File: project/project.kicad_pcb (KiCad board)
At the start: 2 copper layers, 313 parts, among them J101 XT-IN, J102 IN, J103 5V, J104 OUT, J1501 RJ45_LED_Shielded_x2, J201 RJ45_LED_Shielded_x2, J2801 RJ45_LED_Shielded_x2, Q1001 AO3400A, Q101 HYG210P06LQ1D, Q1101 AO3400A, Q1201 AO3400A, Q1301 AO3400A, Q1401 AO3400A, Q1601 AO3400A, Q1701 AO3400A, Q1801 AO3400A, Q1901 AO3400A, Q2001 AO3400A, Q2101 AO3400A, Q2201 AO3400A, Q2301 AO3400A, Q2401 AO3400A, Q2501 AO3400A, Q2601 AO3400A, Q2701 AO3400A, Q2901 AO3400A, Q3001 AO3400A, Q301 AO3400A, Q3101 AO3400A, Q3201 AO3400A, Q3301 AO3400A, Q3401 AO3400A, Q3501 AO3400A, Q3601 AO3400A, Q3701 AO3400A, Q3801 AO3400A, Q3901 AO3400A, Q4001 AO3400A, Q401 AO3400A, Q501 AO3400A, Q601 AO3400A, Q701 AO3400A, Q801 AO3400A, Q901 AO3400A, U101 XL4001, U1501 PCA9685PW, U201 PCA9685PW, U2801 PCA9685PW

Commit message: 2ch grouping layout
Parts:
- moved J102 171.4 mm to (428.0, -91.9)
- moved J104 101.9 mm to (270.0, -119.9)
- moved R2804 50.2 mm to (466.9, -39.8)
- moved R2805 41.8 mm to (466.9, -37.8)
- moved R2803 32.5 mm to (479.4, -43.2), turned to 180 degrees
- moved R2802 30.6 mm to (479.4, -41.3), turned to 180 degrees
- moved C2801 11.5 mm to (479.4, -47.1)
- moved R2801 11.4 mm to (479.4, -45.1), turned to 180 degrees
- moved U2801 5.51 mm to (473.0, -42.0)
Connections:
- R1502 pad 2: /_double_port_pwr2/LED12 -> /_double_port_pwr2/LED21
- R1503 pad 2: /_double_port_pwr2/LED11 -> /_double_port_pwr2/LED22
- R1504 pad 2: /_double_port_pwr2/LED22 -> /_double_port_pwr2/LED11
- R1505 pad 2: /_double_port_pwr2/LED21 -> /_double_port_pwr2/LED12
- R202 pad 2: /_double_port_pwr1/LED12 -> /_double_port_pwr1/LED21
- R203 pad 2: /_double_port_pwr1/LED11 -> /_double_port_pwr1/LED22
- R204 pad 2: /_double_port_pwr1/LED22 -> /_double_port_pwr1/LED11
- R205 pad 2: /_double_port_pwr1/LED21 -> /_double_port_pwr1/LED12
- R2802 pad 2: /_double_port_pwr3/LED12 -> /_double_port_pwr3/LED21
- R2803 pad 2: /_double_port_pwr3/LED11 -> /_double_port_pwr3/LED22
- R2804 pad 2: /_double_port_pwr3/LED22 -> /_double_port_pwr3/LED11
- R2805 pad 2: /_double_port_pwr3/LED21 -> /_double_port_pwr3/LED12
- U1501 pad 10: /_double_port_pwr2/_single_channel_pwr_18/IN -> /_double_port_pwr2/_single_channel_pwr_23/IN
- U1501 pad 11: /_double_port_pwr2/_single_channel_pwr_22/IN -> /_double_port_pwr2/_single_channel_pwr_19/IN
- U1501 pad 15: /_double_port_pwr2/_single_channel_pwr_19/IN -> /_double_port_pwr2/_single_channel_pwr_22/IN
- U1501 pad 16: /_double_port_pwr2/_single_channel_pwr_23/IN -> /_double_port_pwr2/_single_channel_pwr_18/IN
- U1501 pad 17: /_double_port_pwr2/_single_channel_pwr_24/IN -> /_double_port_pwr2/_single_channel_pwr_21/IN
- U1501 pad 18: /_double_port_pwr2/_single_channel_pwr_14/IN -> /_double_port_pwr2/_single_channel_pwr_20/IN
- U1501 pad 19: /_double_port_pwr2/_single_channel_pwr_13/IN -> /_double_port_pwr2/_single_channel_pwr_17/IN
- U1501 pad 20: /_double_port_pwr2/_single_channel_pwr_15/IN -> /_double_port_pwr2/_single_channel_pwr_16/IN
- U1501 pad 6: /_double_port_pwr2/_single_channel_pwr_16/IN -> /_double_port_pwr2/_single_channel_pwr_15/IN
- U1501 pad 7: /_double_port_pwr2/_single_channel_pwr_17/IN -> /_double_port_pwr2/_single_channel_pwr_13/IN
- U1501 pad 8: /_double_port_pwr2/_single_channel_pwr_20/IN -> /_double_port_pwr2/_single_channel_pwr_14/IN
- U1501 pad 9: /_double_port_pwr2/_single_channel_pwr_21/IN -> /_double_port_pwr2/_single_channel_pwr_24/IN
- U201 pad 10: /_double_port_pwr1/_single_channel_pwr_18/IN -> /_double_port_pwr1/_single_channel_pwr_23/IN
- U201 pad 11: /_double_port_pwr1/_single_channel_pwr_22/IN -> /_double_port_pwr1/_single_channel_pwr_19/IN
- U201 pad 15: /_double_port_pwr1/_single_channel_pwr_19/IN -> /_double_port_pwr1/_single_channel_pwr_22/IN
- U201 pad 16: /_double_port_pwr1/_single_channel_pwr_23/IN -> /_double_port_pwr1/_single_channel_pwr_18/IN
- U201 pad 17: /_double_port_pwr1/_single_channel_pwr_24/IN -> /_double_port_pwr1/_single_channel_pwr_21/IN
- U201 pad 18: /_double_port_pwr1/_single_channel_pwr_14/IN -> /_double_port_pwr1/_single_channel_pwr_20/IN
- U201 pad 19: /_double_port_pwr1/_single_channel_pwr_13/IN -> /_double_port_pwr1/_single_channel_pwr_17/IN
- U201 pad 20: /_double_port_pwr1/_single_channel_pwr_15/IN -> /_double_port_pwr1/_single_channel_pwr_16/IN
- U201 pad 6: /_double_port_pwr1/_single_channel_pwr_16/IN -> /_double_port_pwr1/_single_channel_pwr_15/IN
- U201 pad 7: /_double_port_pwr1/_single_channel_pwr_17/IN -> /_double_port_pwr1/_single_channel_pwr_13/IN
- U201 pad 8: /_double_port_pwr1/_single_channel_pwr_20/IN -> /_double_port_pwr1/_single_channel_pwr_14/IN
- U201 pad 9: /_double_port_pwr1/_single_channel_pwr_21/IN -> /_double_port_pwr1/_single_channel_pwr_24/IN
- U2801 pad 10: /_double_port_pwr3/_single_channel_pwr_18/IN -> /_double_port_pwr3/_single_channel_pwr_23/IN
- U2801 pad 11: /_double_port_pwr3/_single_channel_pwr_22/IN -> /_double_port_pwr3/_single_channel_pwr_19/IN
- U2801 pad 15: /_double_port_pwr3/_single_channel_pwr_19/IN -> /_double_port_pwr3/_single_channel_pwr_22/IN
- U2801 pad 16: /_double_port_pwr3/_single_channel_pwr_23/IN -> /_double_port_pwr3/_single_channel_pwr_18/IN
- U2801 pad 17: /_double_port_pwr3/_single_channel_pwr_24/IN -> /_double_port_pwr3/_single_channel_pwr_21/IN
- U2801 pad 18: /_double_port_pwr3/_single_channel_pwr_14/IN -> /_double_port_pwr3/_single_channel_pwr_20/IN
- U2801 pad 19: /_double_port_pwr3/_single_channel_pwr_13/IN -> /_double_port_pwr3/_single_channel_pwr_17/IN
- U2801 pad 20: /_double_port_pwr3/_single_channel_pwr_15/IN -> /_double_port_pwr3/_single_channel_pwr_16/IN
- U2801 pad 6: /_double_port_pwr3/_single_channel_pwr_16/IN -> /_double_port_pwr3/_single_channel_pwr_15/IN
- U2801 pad 7: /_double_port_pwr3/_single_channel_pwr_17/IN -> /_double_port_pwr3/_single_channel_pwr_13/IN
- U2801 pad 8: /_double_port_pwr3/_single_channel_pwr_20/IN -> /_double_port_pwr3/_single_channel_pwr_14/IN
- U2801 pad 9: /_double_port_pwr3/_single_channel_pwr_21/IN -> /_double_port_pwr3/_single_channel_pwr_24/IN
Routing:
- net Net-(J2801-Pad12): track 0.00 -> 44.3 mm, vias 0 -> 1
- net Net-(J2801-Pad10): track 0.00 -> 41.2 mm, vias 0 -> 1
- net Net-(J2801-Pad22): track 0.00 -> 38.9 mm, vias 0 -> 1
- net Net-(J2801-Pad24): track 0.00 -> 38.2 mm, vias 0 -> 1
- net /_double_port_pwr3/_single_channel_pwr_16/IN: track 0.00 -> 32.2 mm
- net /_double_port_pwr3/_single_channel_pwr_17/IN: track 0.00 -> 26.9 mm
- net /_double_port_pwr3/_single_channel_pwr_13/IN: track 9.28 -> 31.6 mm, vias 0 -> 2
- net /_double_port_pwr3/_single_channel_pwr_15/IN: track 5.14 -> 25.8 mm
- net +5V: track 0.00 -> 16.1 mm
- net /_double_port_pwr3/_single_channel_pwr_20/IN: track 0.00 -> 10.8 mm
- net /_double_port_pwr3/_single_channel_pwr_23/IN: track 0.00 -> 8.60 mm
- net /_double_port_pwr3/_single_channel_pwr_14/IN: track 5.34 -> 13.7 mm
- net /_double_port_pwr3/_single_channel_pwr_24/IN: track 2.88 -> 11.0 mm
- net /_double_port_pwr3/_single_channel_pwr_21/IN: track 0.00 -> 7.18 mm
- net /_double_port_pwr3/_single_channel_pwr_19/IN: track 0.00 -> 5.37 mm
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
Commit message: more layout
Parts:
- removed D101: LED-R, LED_SMD:LED_0805_2012Metric_Pad1.15x1.40mm_HandSolder
- removed D103: LED-G, LED_SMD:LED_0805_2012Metric_Pad1.15x1.40mm_HandSolder
- removed D106: GREEN, LED_SMD:LED_0805_2012Metric_Pad1.15x1.40mm_HandSolder
- added C3: 220u/35v, Capacitor_SMD:CP_Elec_10x10, F.Cu at (152.0, 75.0)
- added C4: 220u/35v, Capacitor_SMD:CP_Elec_10x10, F.Cu at (163.0, 75.0)
- added C5: 10u/35v, Capacitor_SMD:C_1206_3216Metric, F.Cu at (137.0, 68.0)
- added D1: LED-R, LED_SMD:LED_0805_2012Metric_Pad1.15x1.40mm_HandSolder, F.Cu at (122.0, 54.0)
- added D3: LED-G, LED_SMD:LED_0805_2012Metric_Pad1.15x1.40mm_HandSolder, F.Cu at (116.0, 54.0)
- added D6: LED-G, LED_SMD:LED_0805_2012Metric_Pad1.15x1.40mm_HandSolder, F.Cu at (185.0, 54.0)
- added H6: MP, MountingHole:MountingHole_3.2mm_M3_Pad_Via, F.Cu at (183.0, 132.5)
- U1: renamed from U101; footprint -local:Texas_HTSOP-8-1EP_3.9x4.9mm_P1.27mm_EP2.8x4.1mm_Mask2.8x4.1mm_ThermalVias -> Package_SO:Texas_HTSOP-8-1EP_3.9x4.9mm_P1.27mm_EP2.95x4.9mm_Mask2.4x3.1mm_ThermalVias
- moved H4 383.8 mm to (117.1, 132.5)
- moved J2 352.5 mm to (115.7, 71.6)
- moved C100 323.6 mm to (184.3, 123.9)
- moved C101 323.6 mm to (184.3, 120.1)
- moved C102 323.6 mm to (187.5, 110.5)
- moved C108 323.6 mm to (177.3, 110.5)
- moved C111 323.6 mm to (173.9, 110.5)
- moved C114 323.6 mm to (170.5, 110.5)
- moved C118 323.6 mm to (168.4, 100.3)
- moved C119 323.6 mm to (168.4, 96.5)
- moved C121 323.6 mm to (171.9, 100.3)
- moved C122 323.6 mm to (171.9, 96.5)
- moved C93 323.6 mm to (194.3, 110.5)
- moved C96 323.6 mm to (190.9, 110.5)
- moved C99 323.6 mm to (184.1, 110.5)
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- renumbered C101 to C1, C107 to C10, C3302 to C100, C3303 to C101, C3401 to C102, C3402 to C103, C3403 to C104, C3501 to C105, C3502 to C106, C3503 to C107, C3601 to C108, C3602 to C109, C108 to C11, C3603 to C110, C3701 to C111, C3702 to C112, C3703 to C113, C3801 to C114, C3802 to C115, C3803 to C116, C3901 to C117, C3902 to C118, C3903 to C119, C201 to C12, C4001 to C120, C4002 to C121, C4003 to C122, C301 to C13, C302 to C14, C303 to C15, C401 to C16, C402 to C17, C403 to C18, C501 to C19, C102 to C2, C502 to C20, C503 to C21, C601 to C22, C602 to C23, C603 to C24, C701 to C25, C702 to C26, C703 to C27, C801 to C28, C802 to C29, C803 to C30, C901 to C31, C902 to C32, C903 to C33, C1001 to C34, C1002 to C35, C1003 to C36, C1101 to C37, C1102 to C38, C1103 to C39, C1201 to C40, C1202 to C41, C1203 to C42, C1301 to C43, C1302 to C44, C1303 to C45, C1401 to C46, C1402 to C47, C1403 to C48, C1501 to C49, C1601 to C50, C1602 to C51, C1603 to C52, C1701 to C53, C1702 to C54, C1703 to C55, C1801 to C56, C1802 to C57, C1803 to C58, C1901 to C59, C103 to C6, C1902 to C60, C1903 to C61, C2001 to C62, C2002 to C63, C2003 to C64, C2101 to C65, C2102 to C66, C2103 to C67, C2201 to C68, C2202 to C69, C104 to C7, C2203 to C70, C2301 to C71, C2302 to C72, C2303 to C73, C2401 to C74, C2402 to C75, C2403 to C76, C2501 to C77, C2502 to C78, C2503 to C79, C105 to C8, C2601 to C80, C2602 to C81, C2603 to C82, C2701 to C83, C2702 to C84, C2703 to C85, C2801 to C86, C2901 to C87, C2902 to C88, C2903 to C89, C106 to C9, C3001 to C90, C3002 to C91, C3003 to C92, C3101 to C93, C3102 to C94, C3103 to C95, C3201 to C96, C3202 to C97, C3203 to C98, C3301 to C99, D601 to D10, D701 to D11, D801 to D12, D901 to D13, D1001 to D14, D1101 to D15, D1201 to D16, D1301 to D17, D1401 to D18, D1601 to D19, D102 to D2, D1701 to D20, D1801 to D21, D1901 to D22, D2001 to D23, D2101 to D24, D2201 to D25, D2301 to D26, D2401 to D27, D2501 to D28, D2601 to D29, D2701 to D30, D2901 to D31, D3001 to D32, D3101 to D33, D3201 to D34, D3301 to D35, D3401 to D36, D3501 to D37, D3601 to D38, D3701 to D39, D104 to D4, D3801 to D40, D3901 to D41, D4001 to D42, D105 to D5, D301 to D7, D401 to D8, D501 to D9, F101 to F1, G101 to G1, G102 to G2, H101 to H1, H102 to H2, H103 to H3, H104 to H4, H105 to H5, J101 to J1, J102 to J2, J103 to J3, J104 to J4, J201 to J5, J1501 to J6, J2801 to J7, L101 to L1, Q101 to Q1, Q1101 to Q10, Q1201 to Q11, Q1301 to Q12, Q1401 to Q13, Q1601 to Q14, Q1701 to Q15, Q1801 to Q16, Q1901 to Q17, Q2001 to Q18, Q2101 to Q19, Q301 to Q2, Q2201 to Q20, Q2301 to Q21, Q2401 to Q22, Q2501 to Q23, Q2601 to Q24, Q2701 to Q25, Q2901 to Q26, Q3001 to Q27, Q3101 to Q28, Q3201 to Q29, Q401 to Q3, Q3301 to Q30, Q3401 to Q31, Q3501 to Q32, Q3601 to Q33, Q3701 to Q34, Q3801 to Q35, Q3901 to Q36, Q4001 to Q37, Q501 to Q4, Q601 to Q5, Q701 to Q6, Q801 to Q7, Q901 to Q8, Q1001 to Q9, R101 to R1, R204 to R10, R203 to R11, R202 to R12, R301 to R13, R302 to R14, R401 to R15, R402 to R16, R501 to R17, R502 to R18, R601 to R19, R102 to R2, R602 to R20, R701 to R21, R702 to R22, R801 to R23, R802 to R24, R901 to R25, R902 to R26, R1001 to R27, R1002 to R28, R1101 to R29, R103 to R3, R1102 to R30, R1201 to R31, R1202 to R32, R1301 to R33, R1302 to R34, R1401 to R35, R1402 to R36, R1501 to R37, R1505 to R38, R1504 to R39, R104 to R4, R1503 to R40, R1502 to R41, R1601 to R42, R1602 to R43, R1701 to R44, R1702 to R45, R1801 to R46, R1802 to R47, R1901 to R48, R1902 to R49, R105 to R5, R2001 to R50, R2002 to R51, R2101 to R52, R2102 to R53, R2201 to R54, R2202 to R55, R2301 to R56, R2302 to R57, R2401 to R58, R2402 to R59, R106 to R6, R2501 to R60, R2502 to R61, R2601 to R62, R2602 to R63, R2701 to R64, R2702 to R65, R2801 to R66, R2805 to R67, R2804 to R68, R2803 to R69, R107 to R7, R2802 to R70, R2901 to R71, R2902 to R72, R3001 to R73, R3002 to R74, R3101 to R75, R3102 to R76, R3201 to R77, R3202 to R78, R3301 to R79, R201 to R8, R3302 to R80, R3401 to R81, R3402 to R82, R3501 to R83, R3502 to R84, R3601 to R85, R3602 to R86, R3701 to R87, R3702 to R88, R3801 to R89, R205 to R9, R3802 to R90, R3901 to R91, R3902 to R92, R4001 to R93, R4002 to R94, RV101 to RV1, U201 to U2, U1501 to U3, U2801 to U4
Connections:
- J2 pad 11: A3 -> +5V
- J4 pad 11: A2 -> unconnected-(J4-Pad11)
- J4 pad 5: GND -> A1
- J4 pad 7: A0 -> A2
- J4 pad 9: A1 -> GND
- J5 pad SH: unconnected-(J201-PadSH) -> GND
- J6 pad SH: unconnected-(J1501-PadSH) -> GND
- J7 pad SH: unconnected-(J2801-PadSH) -> GND
- R7 pad 1: GND -> Net-(R7-Pad1)
- R7 pad 2: Net-(D106-Pad1) -> /VOUTp
- U2 pad 24: +5V -> GND
- U2 pad 4: A3 -> GND
- U3 pad 4: A3 -> GND
- U4 pad 4: A3 -> GND
- U4 pad 5: +5V -> GND
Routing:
- net /_double_port_pwr1/2TBD: track 0.00 -> 60.1 mm
- net /_double_port_pwr1/1Red: track 0.00 -> 57.9 mm
- net /_double_port_pwr1/1white1: track 0.00 -> 57.8 mm
- net /_double_port_pwr1/2White2: track 0.00 -> 57.6 mm
- net Net-(J6-Pad12): track 0.00 -> 44.3 mm, vias 0 -> 1
- net Net-(J5-Pad12): track 0.00 -> 44.3 mm, vias 0 -> 1
- net Net-(J6-Pad10): track 0.00 -> 41.2 mm, vias 0 -> 1
- net Net-(J5-Pad10): track 0.00 -> 41.2 mm, vias 0 -> 1
- net Net-(J5-Pad22): track 0.00 -> 38.9 mm, vias 0 -> 1
- net Net-(J6-Pad22): track 0.00 -> 38.9 mm, vias 0 -> 1
- net Net-(J6-Pad24): track 0.00 -> 38.2 mm, vias 0 -> 1
- net Net-(J5-Pad24): track 0.00 -> 38.2 mm, vias 0 -> 1
- net /_double_port_pwr1/1TBD: track 0.00 -> 35.9 mm
- net /_double_port_pwr1/2white1: track 0.00 -> 33.6 mm
- net /_double_port_pwr2/_single_channel_pwr_16/IN: track 0.00 -> 32.2 mm
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- added copper zone on B.Cu, net +24V
- added copper zone on F.Cu, net +24V
- added copper zone on F.Cu, net /VIN
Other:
- board outline added: 100 x 100 mm
- board text added: "24V OK"
- board text added: "5V OK"
- board text added: "REVERSE POWER!"

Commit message: prepared for production
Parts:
- added REF**: toolhole, -local:toolhole, F.Cu at (191.0, 52.0)
- added REF**: toolhole, -local:toolhole, F.Cu at (103.0, 132.0)
- added REF**: toolhole, -local:toolhole, F.Cu at (109.0, 52.0)
- added kibuzzard-6785251C: G***, kibuzzard-6785251C, F.Cu at (194.0, 60.0)
- added kibuzzard-67852576: G***, kibuzzard-67852576, F.Cu at (106.0, 60.0)
- added kibuzzard-67852857: G***, kibuzzard-67852857, F.Cu at (141.0, 80.0)
- moved G2 53.7 mm to (145.5, 91.0)
- moved C3 46.1 mm to (106.0, 71.5)
- moved G1 42.7 mm to (154.0, 89.0)
- moved C4 31.2 mm to (194.0, 71.5)
- moved C6 28.3 mm to (157.7, 64.7)
- moved C9 28.3 mm to (166.4, 53.7)
- moved D4 28.3 mm to (153.4, 62.2)
- moved L1 28.3 mm to (170.7, 62.1)
- moved R6 28.3 mm to (168.5, 53.7)
- moved R7 28.3 mm to (177.7, 53.7)
- moved C10 28.3 mm to (173.1, 53.1)
- moved C11 28.3 mm to (170.7, 53.1)
- moved C8 28.3 mm to (175.5, 53.1)
- moved C7 28.3 mm to (157.7, 62.3)
- moved D5 28.3 mm to (161.9, 64.5)
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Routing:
- net +5V: track 17.8 -> 188.1 mm, vias 0 -> 6
- net A2: track 0.00 -> 151.8 mm, vias 0 -> 3
- net A1: track 0.00 -> 140.9 mm, vias 0 -> 3
- net SCL: track 0.00 -> 128.6 mm, vias 0 -> 3
- net SDA: track 0.00 -> 121.5 mm
- net A0: track 0.00 -> 118.6 mm, vias 0 -> 6
- net +24V: track 46.3 -> 72.2 mm, vias 144 -> 309
- net Net-(C1-Pad1): track 0.00 -> 18.0 mm
- net GND: track 227.2 -> 242.5 mm, vias 519 -> 566
- net /FB: track 0.00 -> 13.9 mm
- net /VOUTp: track 0.00 -> 8.63 mm
- net Net-(R7-Pad1): track 0.00 -> 7.39 mm
- net Net-(R1-Pad2): track 0.00 -> 6.04 mm
- net Net-(J6-Pad10): track 41.2 -> 46.4 mm, vias 1 -> 2
- net Net-(J5-Pad10): track 41.2 -> 46.4 mm, vias 1 -> 2
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- added copper zone on In2.Cu, net +24V
- added copper zone on F.Cu, net /SW
- added copper zone on B.Cu, net /VIN
- added copper zone on F.Cu, net /VINp
- added copper zone on F.Cu, net /VOUTp
- added copper zone on B.Cu, net GND
- added copper zone on F.Cu, net GND
- added copper zone on In1.Cu, net GND
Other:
- outline, holes or cut-outs redrawn
- copper layers 2 -> 4
- board text added: "JLCJLCJLCJLC"

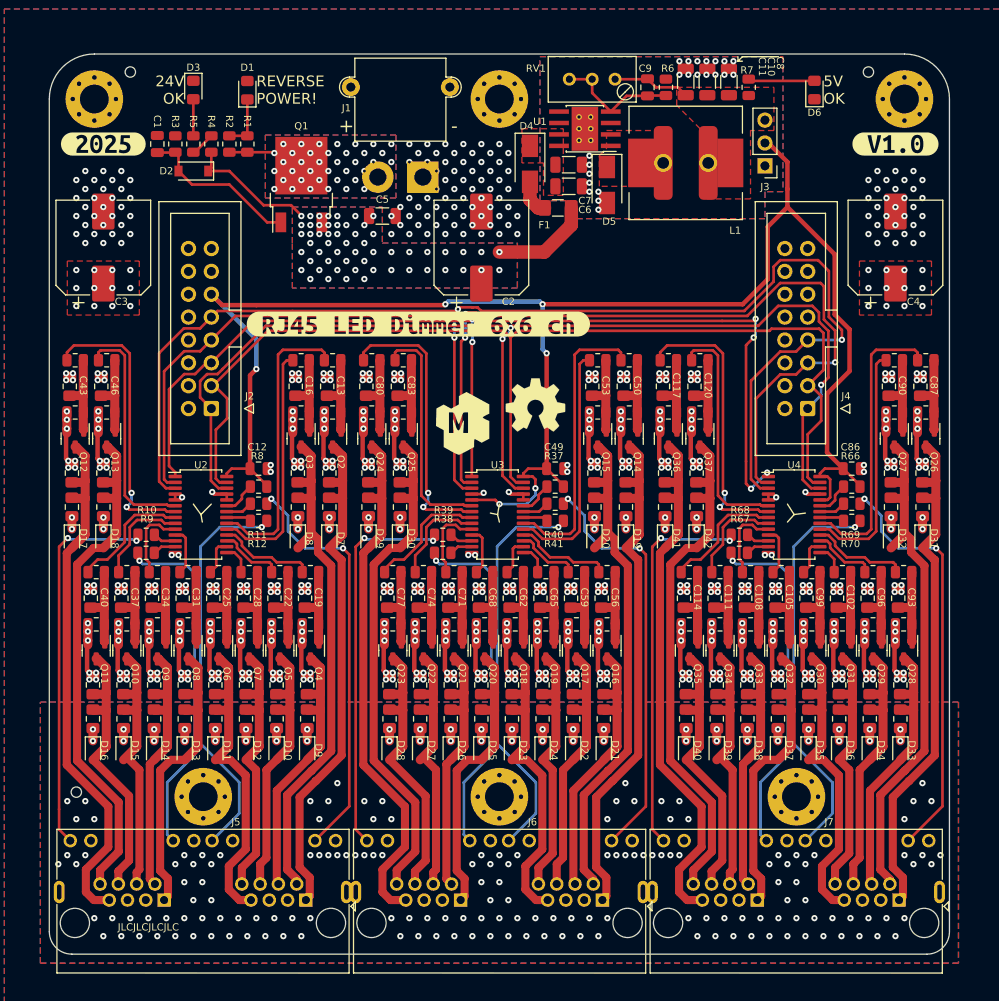
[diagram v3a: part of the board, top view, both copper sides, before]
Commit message: improvements after first prototype test
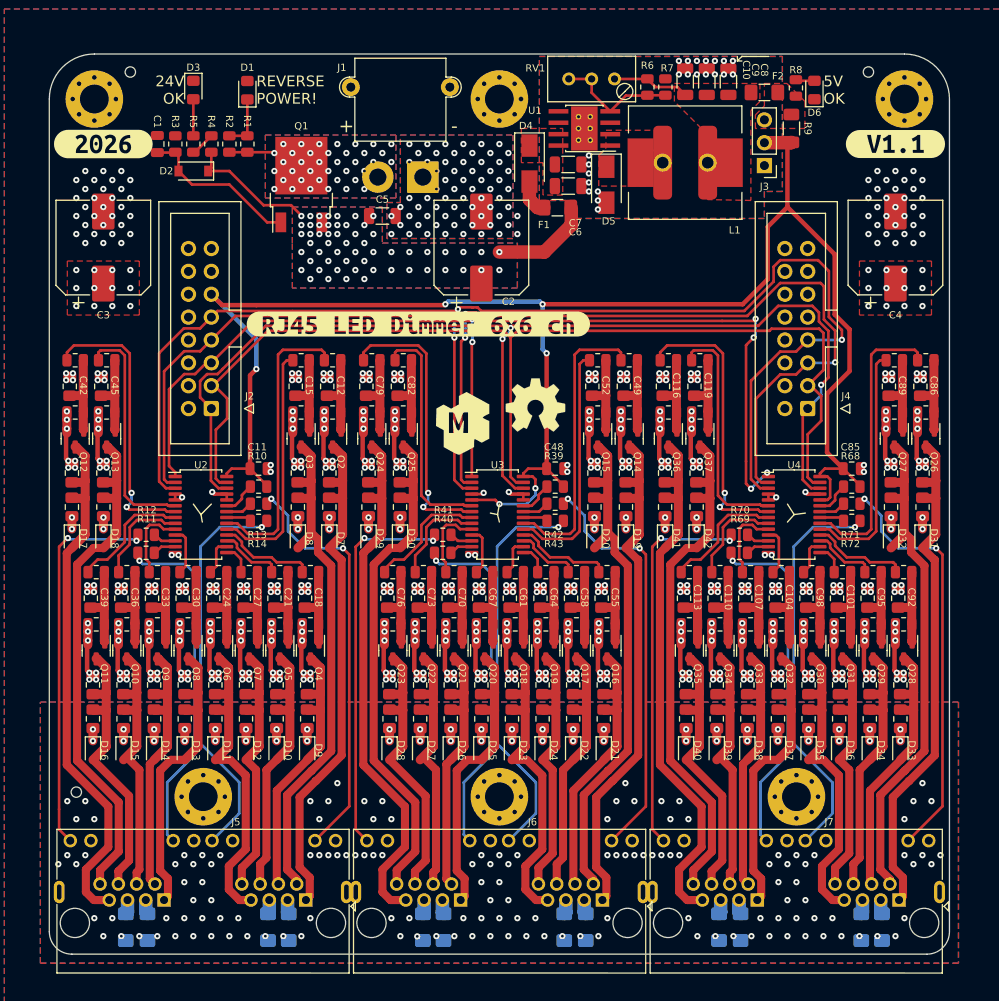
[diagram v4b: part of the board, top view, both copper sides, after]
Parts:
- removed the C9 at (166.4, 53.7)
- removed kibuzzard-6785251C: G***, kibuzzard-6785251C
- removed kibuzzard-67852576: G***, kibuzzard-67852576
- added F10: 1A, Fuse:Fuse_1206_3216Metric_Pad1.42x1.75mm_HandSolder, B.Cu at (159.6, 147.0)
- added F11: 1A, Fuse:Fuse_1206_3216Metric_Pad1.42x1.75mm_HandSolder, B.Cu at (174.4, 147.0)
- added F12: 1A, Fuse:Fuse_1206_3216Metric_Pad1.42x1.75mm_HandSolder, B.Cu at (176.8, 147.0)
- added F13: 1A, Fuse:Fuse_1206_3216Metric_Pad1.42x1.75mm_HandSolder, B.Cu at (190.2, 147.0)
- added F14: 1A, Fuse:Fuse_1206_3216Metric_Pad1.42x1.75mm_HandSolder, B.Cu at (192.5, 147.0)
- added F2: 300mA, Fuse:Fuse_1206_3216Metric_Pad1.42x1.75mm_HandSolder, F.Cu at (179.4, 54.3)
- added F3: 1A, Fuse:Fuse_1206_3216Metric_Pad1.42x1.75mm_HandSolder, B.Cu at (108.5, 147.0)
- added F4: 1A, Fuse:Fuse_1206_3216Metric_Pad1.42x1.75mm_HandSolder, B.Cu at (110.9, 147.0)
- added F5: 1A, Fuse:Fuse_1206_3216Metric_Pad1.42x1.75mm_HandSolder, B.Cu at (124.3, 147.0)
- added F6: 1A, Fuse:Fuse_1206_3216Metric_Pad1.42x1.75mm_HandSolder, B.Cu at (126.6, 147.0)
- added F7: 1A, Fuse:Fuse_1206_3216Metric_Pad1.42x1.75mm_HandSolder, B.Cu at (141.5, 147.0)
- added F8: 1A, Fuse:Fuse_1206_3216Metric_Pad1.42x1.75mm_HandSolder, B.Cu at (143.8, 147.0)
- added F9: 1A, Fuse:Fuse_1206_3216Metric_Pad1.42x1.75mm_HandSolder, B.Cu at (157.2, 147.0)
- added R6: 4k7, Resistor_SMD:R_0805_2012Metric, F.Cu at (166.4, 53.7)
- added R9: 0R1, Resistor_SMD:R_1206_3216Metric_Pad1.30x1.75mm_HandSolder, F.Cu at (182.4, 58.3)
- added kibuzzard-69BFE35C: G***, kibuzzard-69BFE35C, F.Cu at (194.0, 60.0)
- added kibuzzard-69BFE365: G***, kibuzzard-69BFE365, F.Cu at (106.0, 60.0)
- D10, D11, D12, D13, D14, D15, D16, D17, D18, D19, D20, D21, D22, D23, D24, D25, D26, D27, D28, D29, D30, D31, D32, D33, D34, D35, D36, D37, D38, D39, D40, D41, D42, D7, D8, D9: value B5819WS -> 1N5819WS
- D2: value 10V -> 11V
- D4, D5: value SS34A -> SS34
- F1: value 1A -> 100mA
- R10: renamed from R8; value 10K -> 10k
- R39: renamed from R37; value 10K -> 10k
- R4, R5: value 10K -> 10k
- R68: renamed from R66; value 10K -> 10k
- moved R8 5.24 mm to (182.9, 53.8)
- moved C10 0.07 mm to (170.6, 53.1)
- moved C6 0.07 mm to (157.6, 64.7)
- moved C8 0.07 mm to (175.4, 53.1)
- moved C9 0.07 mm to (173.0, 53.1)
- moved D4 0.07 mm to (153.3, 62.2)
- moved D5 0.07 mm to (161.9, 64.5)
- moved F1 0.07 mm to (156.4, 67.1)
- moved L1 0.07 mm to (170.6, 62.1)
- moved R7 0.07 mm to (168.4, 53.7)
- moved C7 0.07 mm to (157.6, 62.3)
- moved J3 0.07 mm to (179.4, 62.4)
- moved RV1 0.07 mm to (162.8, 52.8)
- moved U1 0.07 mm to (159.4, 58.3)
- renumbered C11 to C10, C101 to C100, C102 to C101, C103 to C102, C104 to C103, C105 to C104, C106 to C105, C107 to C106, C108 to C107, C109 to C108, C110 to C109, C12 to C11, C111 to C110, C112 to C111, C113 to C112, C114 to C113, C115 to C114, C116 to C115, C117 to C116, C118 to C117, C119 to C118, C120 to C119, C13 to C12, C121 to C120, C122 to C121, C14 to C13, C15 to C14, C16 to C15, C17 to C16, C18 to C17, C19 to C18, C20 to C19, C21 to C20, C22 to C21, C23 to C22, C24 to C23, C25 to C24, C26 to C25, C27 to C26, C28 to C27, C29 to C28, C30 to C29, C31 to C30, C32 to C31, C33 to C32, C34 to C33, C35 to C34, C36 to C35, C37 to C36, C38 to C37, C39 to C38, C40 to C39, C41 to C40, C42 to C41, C43 to C42, C44 to C43, C45 to C44, C46 to C45, C47 to C46, C48 to C47, C49 to C48, C50 to C49, C51 to C50, C52 to C51, C53 to C52, C54 to C53, C55 to C54, C56 to C55, C57 to C56, C58 to C57, C59 to C58, C60 to C59, C61 to C60, C62 to C61, C63 to C62, C64 to C63, C65 to C64, C66 to C65, C67 to C66, C68 to C67, C69 to C68, C70 to C69, C71 to C70, C72 to C71, C73 to C72, C74 to C73, C75 to C74, C76 to C75, C77 to C76, C78 to C77, C79 to C78, C80 to C79, C81 to C80, C82 to C81, C83 to C82, C84 to C83, C85 to C84, C86 to C85, C87 to C86, C88 to C87, C89 to C88, C90 to C89, C10 to C9, C91 to C90, C92 to C91, C93 to C92, C94 to C93, C95 to C94, C96 to C95, C97 to C96, C98 to C97, C99 to C98, C100 to C99, R9 to R11, R10 to R12, R11 to R13, R12 to R14, R13 to R15, R14 to R16, R15 to R17, R16 to R18, R17 to R19, R18 to R20, R19 to R21, R20 to R22, R21 to R23, R22 to R24, R23 to R25, R24 to R26, R25 to R27, R26 to R28, R27 to R29, R28 to R30, R29 to R31, R30 to R32, R31 to R33, R32 to R34, R33 to R35, R34 to R36, R35 to R37, R36 to R38, R38 to R40, R39 to R41, R40 to R42, R41 to R43, R42 to R44, R43 to R45, R44 to R46, R45 to R47, R46 to R48, R47 to R49, R48 to R50, R49 to R51, R50 to R52, R51 to R53, R52 to R54, R53 to R55, R54 to R56, R55 to R57, R56 to R58, R57 to R59, R58 to R60, R59 to R61, R60 to R62, R61 to R63, R62 to R64, R63 to R65, R64 to R66, R65 to R67, R67 to R69, R6 to R7, R68 to R70, R69 to R71, R70 to R72, R71 to R73, R72 to R74, R73 to R75, R74 to R76, R75 to R77, R76 to R78, R77 to R79, R7 to R8, R78 to R80, R79 to R81, R80 to R82, R81 to R83, R82 to R84, R83 to R85, R84 to R86, R85 to R87, R86 to R88, R87 to R89, R88 to R90, R89 to R91, R90 to R92, R91 to R93, R92 to R94, R93 to R95, R94 to R96
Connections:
- J3 pad 3: /VOUTp -> /VOUTf
- J5 pad 15: +24V -> Net-(F4-Pad2)
- J5 pad 17: +24V -> Net-(F3-Pad2)
- J5 pad 3: +24V -> Net-(F6-Pad2)
- J5 pad 5: +24V -> Net-(F5-Pad2)
- J6 pad 15: +24V -> Net-(F8-Pad2)
- J6 pad 17: +24V -> Net-(F7-Pad2)
- J6 pad 3: +24V -> Net-(F10-Pad2)
- J6 pad 5: +24V -> Net-(F9-Pad2)
- J7 pad 15: +24V -> Net-(F12-Pad2)
- J7 pad 17: +24V -> Net-(F11-Pad2)
- J7 pad 3: +24V -> Net-(F14-Pad2)
- J7 pad 5: +24V -> Net-(F13-Pad2)
- R8 pad 2: /VOUTp -> /VOUTf
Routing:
- net Net-(D6-Pad2): track 7.39 -> 2.11 mm
- net +5V: track 188.1 -> 192.3 mm
- net Net-(F9-Pad2): track 0.00 -> 1.60 mm
- net Net-(F3-Pad2): track 0.00 -> 1.60 mm
- net Net-(F11-Pad2): track 0.00 -> 1.60 mm
- net Net-(F12-Pad2): track 0.00 -> 1.60 mm
- net Net-(F4-Pad2): track 0.00 -> 1.60 mm
- net Net-(F10-Pad2): track 0.00 -> 1.60 mm
- net Net-(F13-Pad2): track 0.00 -> 1.58 mm
- net Net-(F5-Pad2): track 0.00 -> 1.58 mm
- net Net-(F7-Pad2): track 0.00 -> 1.58 mm
- net Net-(F8-Pad2): track 0.00 -> 1.58 mm
- net Net-(F14-Pad2): track 0.00 -> 1.58 mm
- net Net-(F6-Pad2): track 0.00 -> 1.58 mm
- net +24V: vias 309 -> 293
- added copper zone on In1.Cu, net /VIN
- added copper zone on In2.Cu, net /VIN
- added copper zone on F.Cu, net /VOUTf
- added copper zone on In2.Cu, net GND
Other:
- board text removed: "JLCJLCJLCJLC"
